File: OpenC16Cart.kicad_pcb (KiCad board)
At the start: 2 copper layers, 52 x 65 mm, 13 parts, among them CN1 C16-Exp-Port, J1 Conn_02x03_Odd_Even, J11 Conn_01x03_Male, J12 Conn_01x03_Male, J21 Conn_01x03_Male, J22 Conn_01x03_Male, J4 Conn_02x03_Odd_Even, U1 27512 - LO ROM, U2 27512 - HI ROM

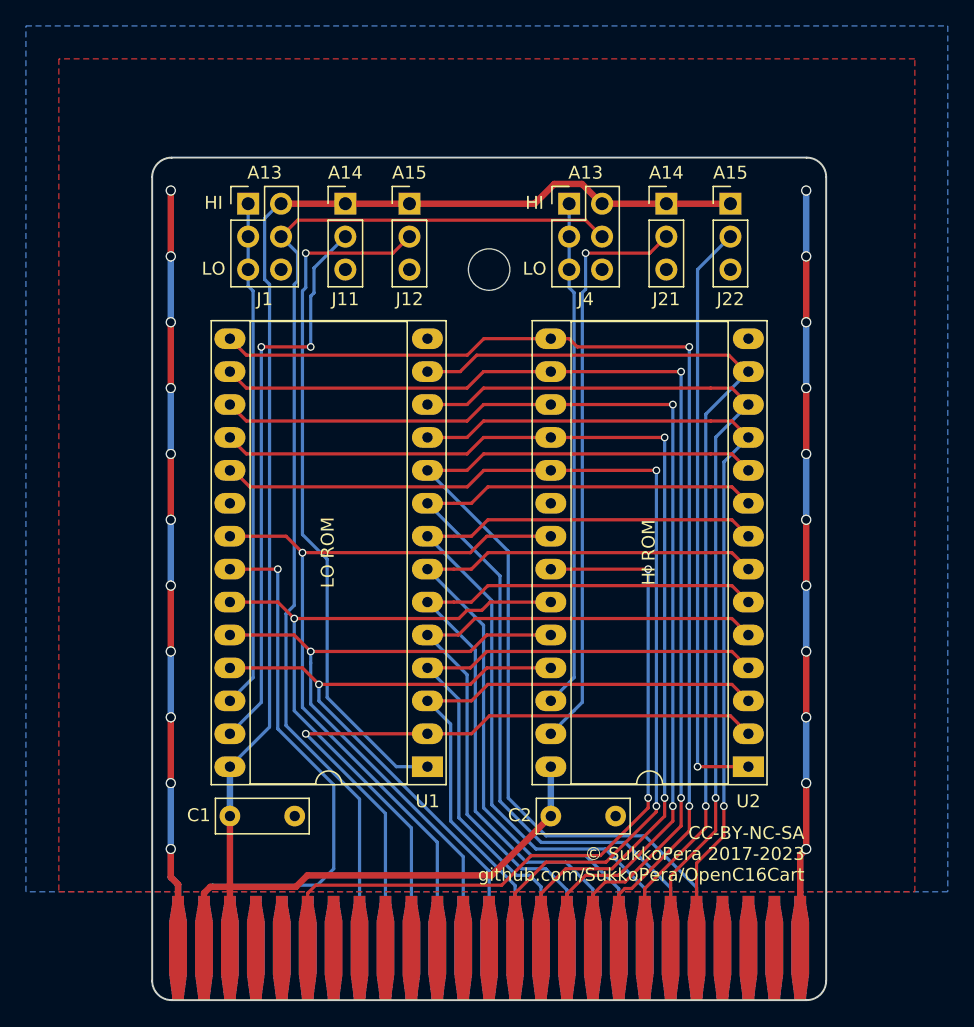
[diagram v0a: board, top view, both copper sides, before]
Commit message: Experimental 16/32/64 KB version with 44-pin 2.54" connector
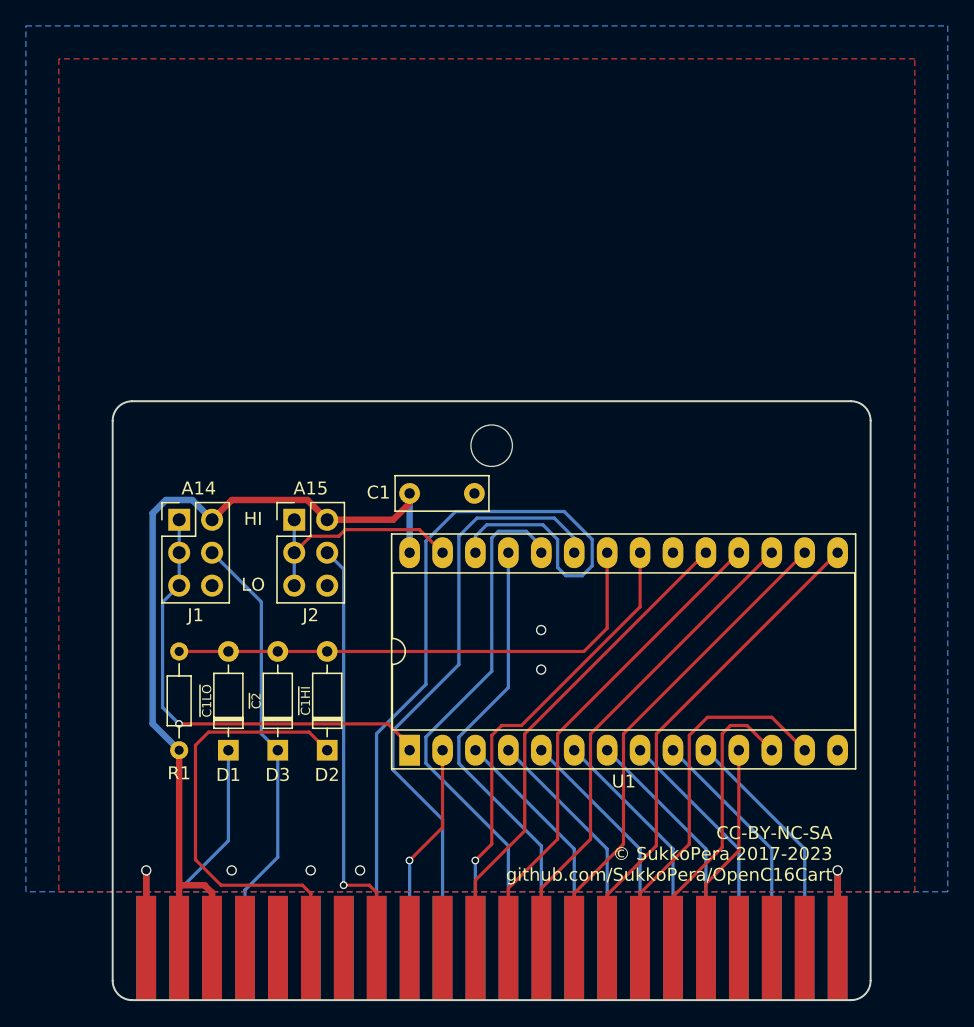
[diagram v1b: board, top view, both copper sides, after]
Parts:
- removed C2: 100n, Capacitor_THT:C_Disc_D7.0mm_W2.5mm_P5.00mm
- removed J11, J12, J21, J22: Conn_01x03_Male, Connector_PinHeader_2.54mm:PinHeader_1x03_P2.54mm_Vertical
- removed J4: Conn_02x03_Odd_Even, Connector_PinHeader_2.54mm:PinHeader_2x03_P2.54mm_Vertical
- removed U2: 27512 - HI ROM, Package_DIP:DIP-28_W15.24mm_Socket_LongPads
- added D1: 1n4148, Diode_THT:D_DO-35_SOD27_P7.62mm_Horizontal, F.Cu at (127.4, 109.2)
- added D2: 1n4148, Diode_THT:D_DO-35_SOD27_P7.62mm_Horizontal, F.Cu at (135.0, 109.2)
- added D3: 1n4148, Diode_THT:D_DO-35_SOD27_P7.62mm_Horizontal, F.Cu at (131.2, 109.2)
- added J2: Conn_02x03_Odd_Even, Connector_PinHeader_2.54mm:PinHeader_2x03_P2.54mm_Vertical, F.Cu at (132.5, 91.4)
- added R1: 3.3k, Resistor_THT:R_Axial_DIN0204_L3.6mm_D1.6mm_P7.62mm_Horizontal, F.Cu at (123.6, 101.6)
- CN1: value C16-Exp-Port -> C16_EXP_PORT_44PIN; footprint OpenC16Cart:C16_Cart_Conn -> OpenC16Cart:C16-Exp-Port-44Pin
- U1: value 27512 - LO ROM -> 27512
- moved CN1 29.3 mm to (118.5, 128.4)
- moved C1 28.5 mm to (141.4, 89.4)
- moved J1 25.0 mm to (123.6, 91.4)
- moved V0 20.9 mm to (157.9, 101.6)
- moved H1 13.6 mm to (147.7, 85.7)
- moved U1 1.87 mm to (141.4, 109.2), turned to 90 degrees
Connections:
- CN1 pad 11: Net-(CN1-Pad11) -> /d7
- CN1 pad 12: Net-(CN1-Pad12) -> /d6
- CN1 pad 13: Net-(CN1-Pad13) -> /d5
- CN1 pad 14: /d7 -> /d4
- CN1 pad 15: /d6 -> /d3
- CN1 pad 16: /d5 -> /d2
- CN1 pad 17: /d4 -> /d1
- CN1 pad 18: /d3 -> /d0
- CN1 pad 19: /d2 -> Net-(CN1-Pad19)
- CN1 pad 20: /d1 -> Net-(CN1-Pad20)
- CN1 pad 21: /d0 -> Net-(CN1-Pad21)
- CN1 pad 22: Net-(CN1-Pad22) -> GND
- CN1 pad 8: Net-(CN1-Pad8) -> /~cs0
- CN1 pad D: Net-(CN1-PadD) -> /~c2
- CN1 pad J: /a13_conn -> /a13
- CN1 pad Z: Net-(CN1-PadZ) -> GND
- J1 pad 1: /a13_u1 -> /rom_a15
- J1 pad 3: /a13_u1 -> /rom_a15
- J1 pad 4: /a13_conn -> /~c2
- J1 pad 5: /a13_u1 -> /rom_a15
- U1 pad 1: /a15_u1 -> /rom_a15
- U1 pad 22: /~c1lo -> /~rom_oe
- U1 pad 26: /a13_u1 -> /a13
- U1 pad 27: /a14_u1 -> /rom_a14
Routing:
- net GND: track 133.1 -> 23.8 mm, vias 22 -> 7
- net /a13_conn: track 84.0 -> 0.00 mm
- net /a13: track 0.00 -> 63.9 mm
- net VCC: track 132.1 -> 68.6 mm
- net /a0: track 75.7 -> 18.4 mm
- net /a15_u1: track 53.7 -> 0.00 mm, vias 1 -> 0
- net /a1: track 71.7 -> 18.4 mm
- net /d0: track 66.9 -> 16.3 mm, vias 1 -> 0
- net /a2: track 67.7 -> 18.4 mm
- net /d3: track 85.8 -> 37.8 mm, vias 2 -> 0
- net /d1: track 70.2 -> 23.0 mm, vias 1 -> 0
- net /d4: track 84.2 -> 37.8 mm, vias 2 -> 0
- net /a15_u2: track 45.9 -> 0.00 mm, vias 1 -> 0
- net /a3: track 63.6 -> 18.4 mm
- net /d2: track 73.6 -> 28.5 mm, vias 1 -> 0
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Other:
- board size 52 x 65 mm -> 58.5 x 46.2 mm
- board text added: "V5"
- board text added: "~C1HI"
- board text added: "~C1LO"
- board text added: "~C2"
- board text removed: "A13"
- board text removed: "HI ROM"
- board text removed: "LO ROM"
- board text removed: "V4"

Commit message: Add logo
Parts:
- added V1: LOGO1, OpenC16Cart:logo1, F.Cu at (126.2, 115.9)
- added V2: LOGO2, OpenC16Cart:logo2, F.Cu at (128.9, 118.7)
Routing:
- net /~cs0: track 33.2 -> 32.1 mm
- net GND: vias 7 -> 8

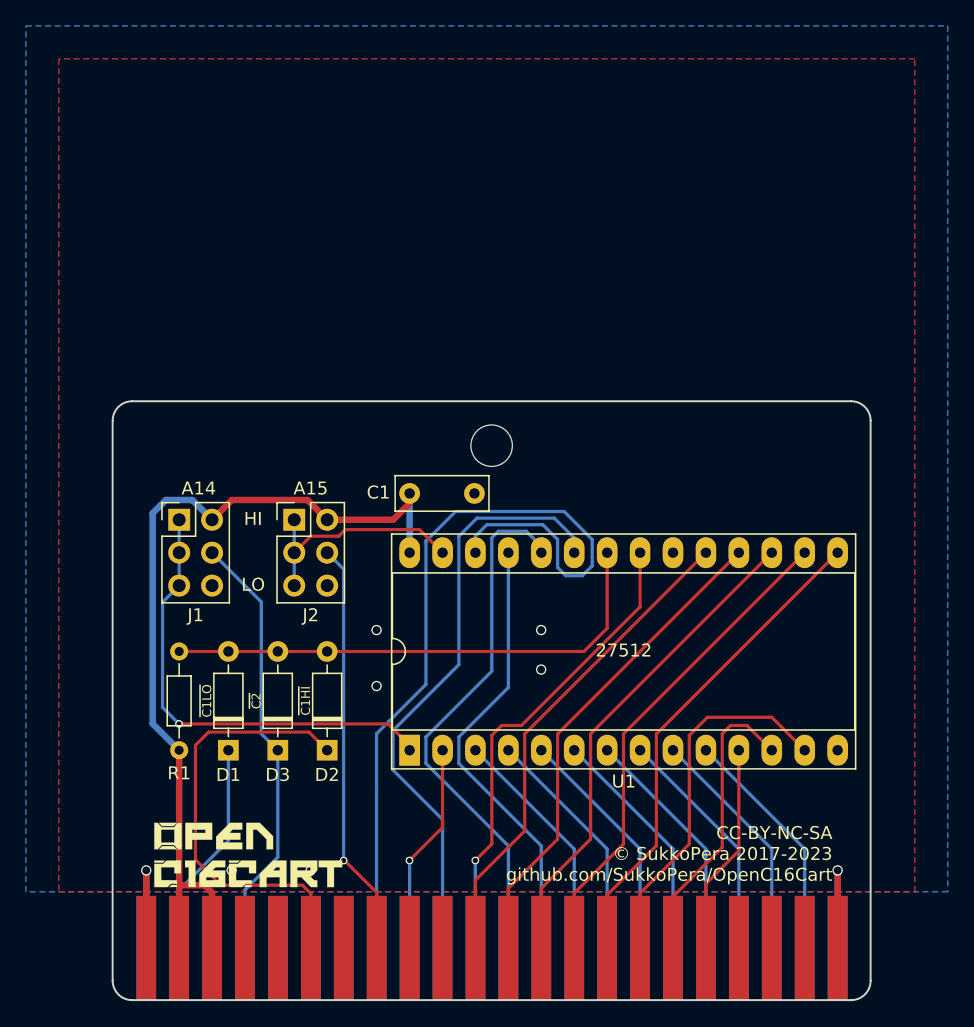
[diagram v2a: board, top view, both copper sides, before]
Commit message: Comply with Stumpy cases dimensions
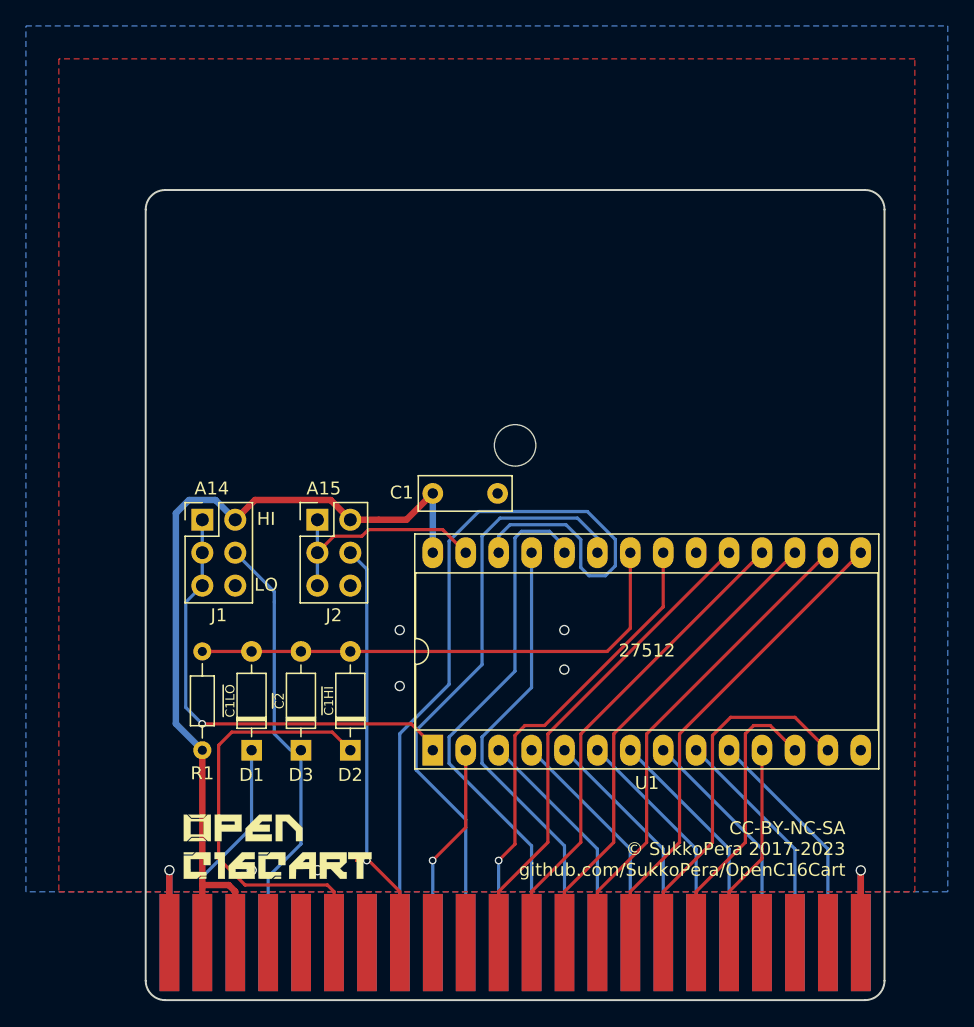
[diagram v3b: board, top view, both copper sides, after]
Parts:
- moved CN1 31.0 mm to (149.5, 128.3)
- moved V1 2.36 mm to (128.5, 115.2)
- moved V2 2.36 mm to (131.2, 118.1)
- moved H1 1.81 mm to (149.5, 85.7)
- moved J1 1.79 mm to (125.4, 91.4)
- moved R1 1.79 mm to (125.4, 101.6)
- moved C1 1.79 mm to (143.2, 89.4)
- moved D1 1.79 mm to (129.2, 109.2)
- moved D2 1.79 mm to (136.8, 109.2)
- moved D3 1.79 mm to (133.0, 109.2)
- moved J2 1.79 mm to (134.2, 91.4)
- moved U1 1.79 mm to (143.2, 109.2)
- moved V0 1.79 mm to (159.7, 101.6)
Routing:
- net /a13: track 63.9 -> 59.9 mm
- net /~c2: track 33.6 -> 32.9 mm
- net /~cs0: track 32.1 -> 32.6 mm
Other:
- board size 58.5 x 46.2 mm -> 57 x 62.5 mm
- board text added: "BUTTON"
- board text added: "RESET"

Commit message: Add reset button
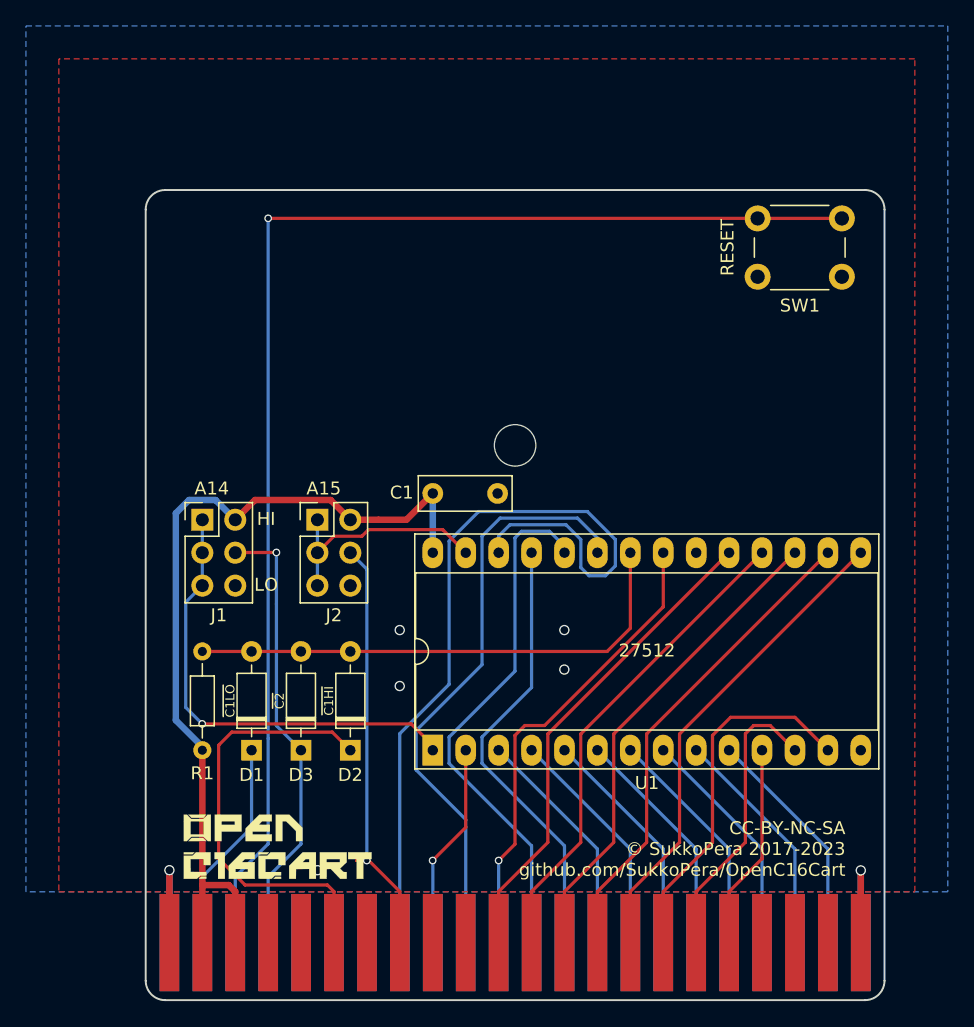
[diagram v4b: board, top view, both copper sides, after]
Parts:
- added SW1: BTN_RESET, Button_Switch_THT:SW_PUSH_6mm_H8mm, F.Cu at (168.2, 68.2)
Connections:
- CN1 pad C: Net-(CN1-PadC) -> /~reset
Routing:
- net /~reset: track 0.00 -> 101.2 mm, vias 0 -> 1
- net /~c2: track 32.9 -> 35.1 mm, vias 0 -> 1
- net GND: vias 8 -> 7

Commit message: Bigger logo and final touches
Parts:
- moved V1 45.2 mm to (137.6, 71.0)
- moved V2 40.8 mm to (146.1, 80.1)
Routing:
- net GND: track 23.8 -> 25.9 mm
- net /~cs0: track 32.6 -> 31.7 mm
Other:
- board text added: "DO *NOT* PLUG THIS CARTRIDGE INTO A C64 OR C128!"

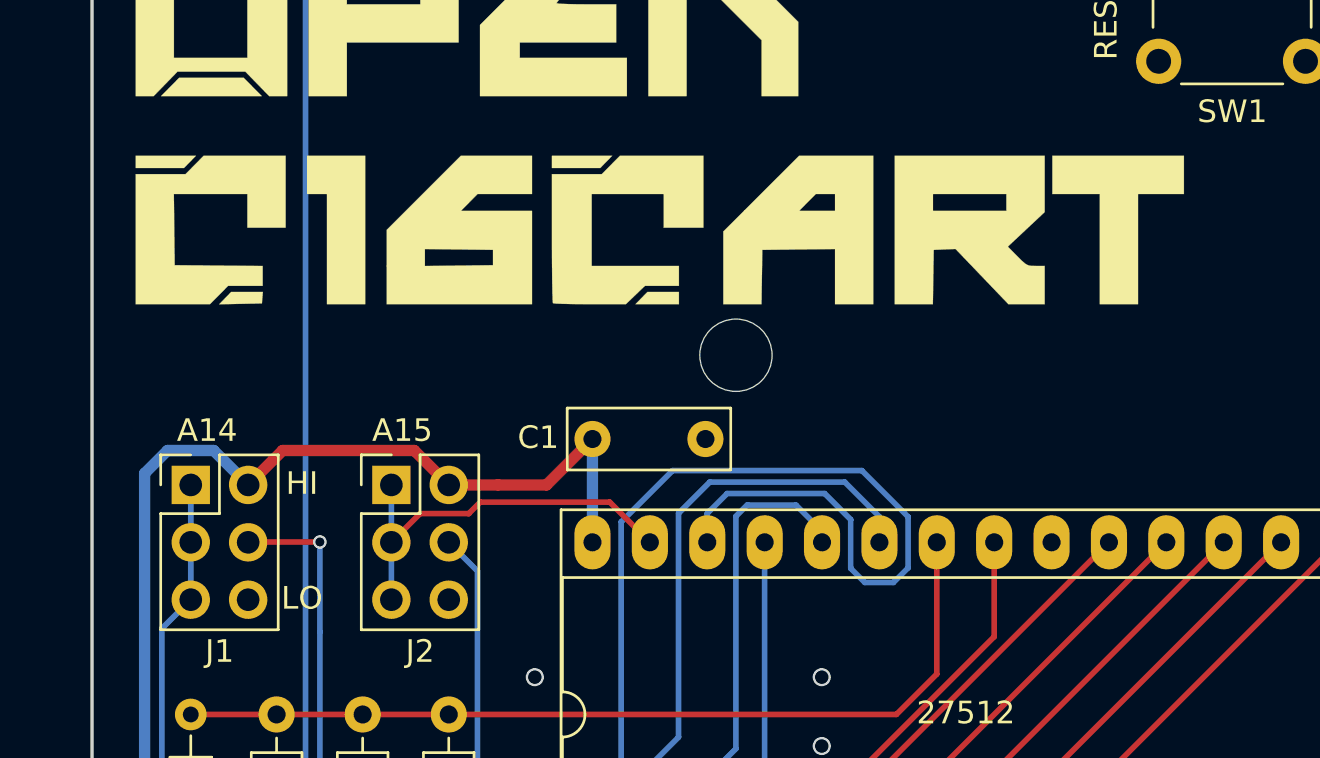
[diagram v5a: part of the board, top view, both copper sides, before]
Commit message: Make hole compliant with Stumpy cases
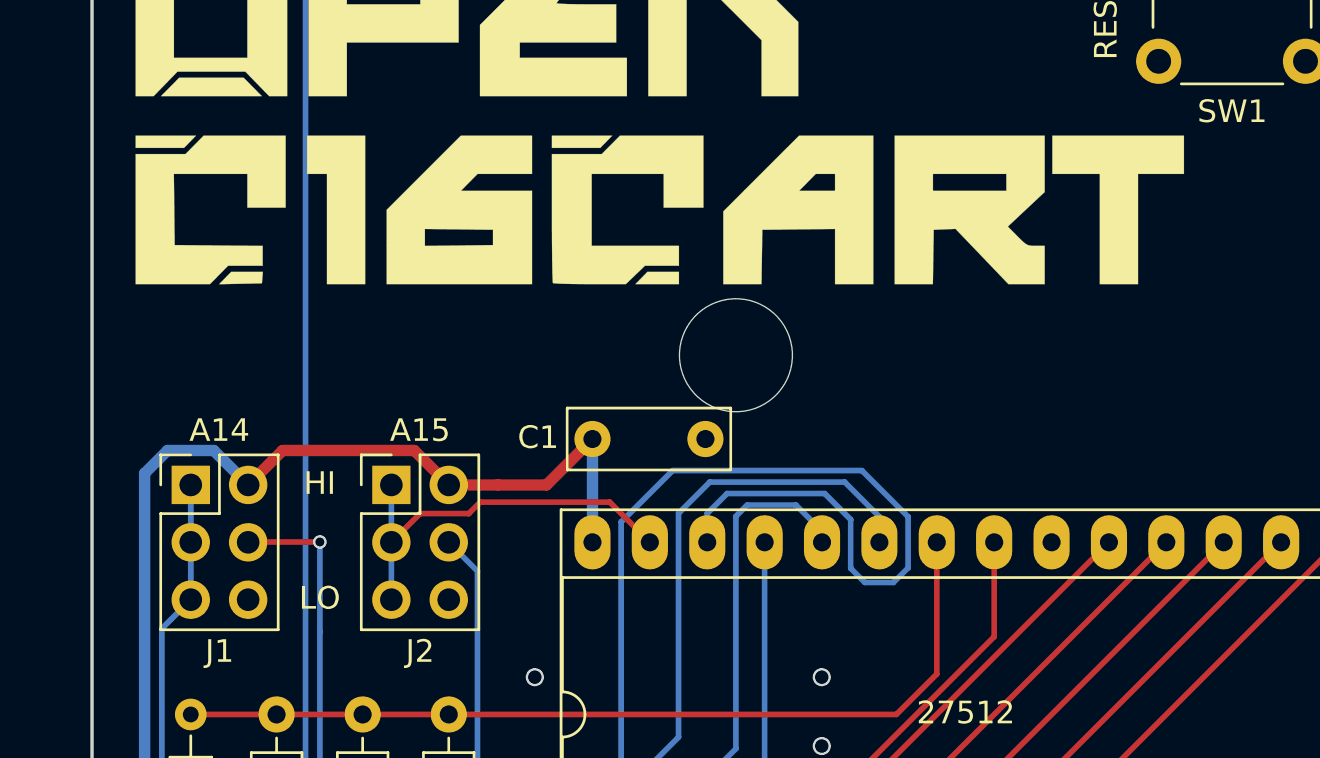
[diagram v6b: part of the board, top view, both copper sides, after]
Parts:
- H1: footprint MountingHole:MountingHole_3.2mm_M3 -> MountingHole:MountingHole_5mm
- moved V2 0.89 mm to (146.1, 79.2)

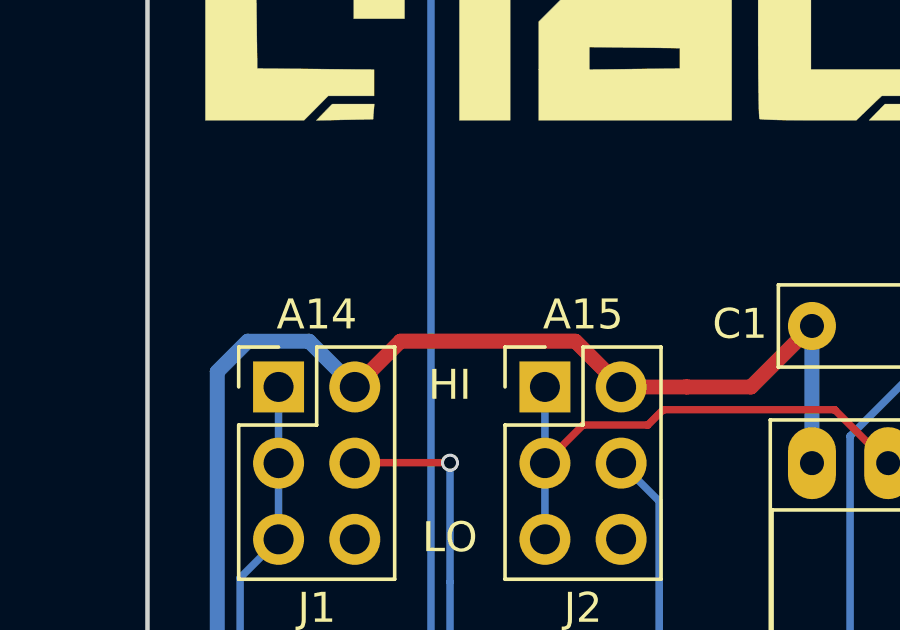
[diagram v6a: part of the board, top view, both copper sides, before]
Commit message: Fix R1 value and A14/15 labels
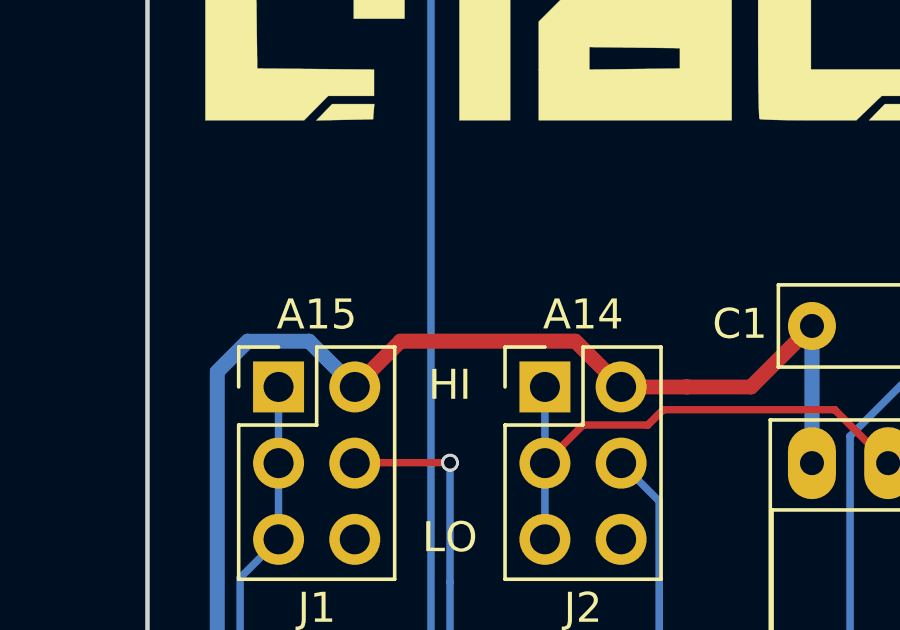
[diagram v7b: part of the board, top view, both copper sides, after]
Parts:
- R1: value 3.3k -> 270

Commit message: Move components bottom left
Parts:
- moved V0 1.80 mm to (158.4, 102.9)
- moved C1 1.80 mm to (141.9, 90.7)
- moved U1 1.80 mm to (141.9, 110.5)
- moved R1 1.27 mm to (125.4, 102.9)
- moved D1 1.27 mm to (129.2, 110.5)
- moved D2 1.27 mm to (136.8, 110.5)
- moved D3 1.27 mm to (133.0, 110.5)
- moved J1 1.27 mm to (125.4, 92.7)
- moved J2 1.27 mm to (134.2, 92.7)
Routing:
- net /a13: track 59.8 -> 62.1 mm
- net VCC: track 69.0 -> 70.9 mm
- net /d1: track 22.6 -> 20.8 mm
- net /d0: track 15.9 -> 14.1 mm
- net /a12: track 15.9 -> 14.1 mm
- net /d6: track 37.4 -> 35.6 mm
- net /d5: track 37.4 -> 35.6 mm
- net /d2: track 28.1 -> 26.3 mm
- net /d7: track 37.4 -> 35.6 mm
- net /d4: track 37.4 -> 35.6 mm
- net /d3: track 37.4 -> 35.6 mm
- net /a10: track 36.2 -> 34.4 mm
- net /~c1hi: track 33.8 -> 32.5 mm
- net /rom_a15: track 35.7 -> 34.4 mm
- net /~cs0: track 31.7 -> 30.4 mm
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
